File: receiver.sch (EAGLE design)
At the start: 32 parts

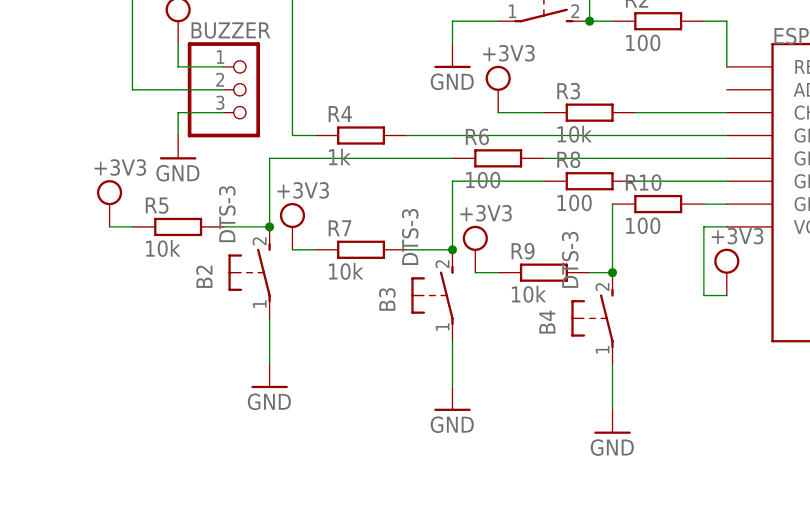
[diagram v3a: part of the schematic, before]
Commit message: Changed 2pins tact switches for 4pins tact switches.
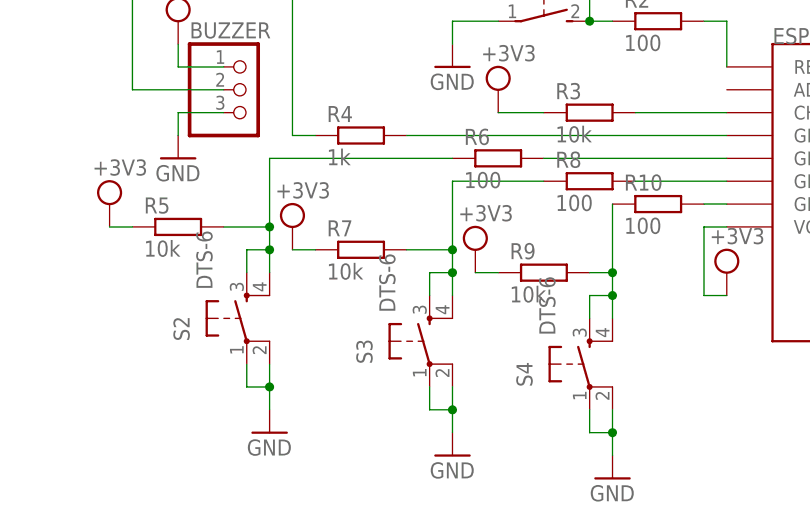
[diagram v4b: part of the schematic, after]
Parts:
- removed B2, B3, B4: DTS-3, switch-tact:DTS-3
- added S2, S3, S4: DTS-6, switch-tact:DTS-6
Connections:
- removed net N$14: B3.2, R7.2, R8.1
- removed net N$8: B4.2, R10.1, R9.2
- new net N$22: R10.1, R9.2, S4.3, S4.4
- new net N$23: R5.2, R6.1, S2.3, S2.4
- net GND: now also S2.1, S2.2, S3.1, S3.2, S4.1, S4.2; no longer B2.1, B3.1, B4.1
- net N$13: now also R7.2, R8.1, S3.3, S3.4; no longer B2.2, R5.2, R6.1
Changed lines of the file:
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@@
 <part name="PROG_USB" library="pinhead" library_urn="urn:adsk.eagle:library:325" deviceset="PINHD-1X4" device="" package3d_urn="urn:adsk.eagle:package:22407/2"/>
 <part name="GND4" library="supply1" library_urn="urn:adsk.eagle:library:371" deviceset="GND" device=""/>
-<part name="B3" library="switch-tact" deviceset="DTS-3" device=""/>
-<part name="B4" library="switch-tact" deviceset="DTS-3" device=""/>
 <part name="R7" library="rcl" library_urn="urn:adsk.eagle:library:334" deviceset="R-EU_" device="0204/5" package3d_urn="urn:adsk.eagle:package:23488/1" value="10k"/>
 <part name="R9" library="rcl" library_urn="urn:adsk.eagle:library:334" deviceset="R-EU_" device="0204/5" package3d_urn="urn:adsk.eagle:package:23488/1" value="10k"/>
@@
 <part name="SUPPLY18" library="supply2" library_urn="urn:adsk.eagle:library:372" deviceset="VCC" device="" value="+3V3"/>
 <part name="SU/SD3V3" library="Pololu Voltage Regulators" deviceset="5V_VOLTAGE_REGULATOR" device=""/>
-<part name="B2" library="switch-tact" deviceset="DTS-3" device=""/>
 <part name="R5" library="rcl" library_urn="urn:adsk.eagle:library:334" deviceset="R-EU_" device="0204/5" package3d_urn="urn:adsk.eagle:package:23488/1" value="10k"/>
 <part name="R6" library="rcl" library_urn="urn:adsk.eagle:library:334" deviceset="R-EU_" device="0204/5" package3d_urn="urn:adsk.eagle:package:23488/1" value="100"/>
@@
 <part name="R14" library="rcl" library_urn="urn:adsk.eagle:library:334" deviceset="R-EU_" device="0204/5" package3d_urn="urn:adsk.eagle:package:23488/1" value="100"/>
 <part name="R2" library="rcl" library_urn="urn:adsk.eagle:library:334" deviceset="R-EU_" device="0204/5" package3d_urn="urn:adsk.eagle:package:23488/1" value="100"/>
+<part name="S2" library="switch-tact" deviceset="DTS-6" device=""/>
+<part name="S3" library="switch-tact" deviceset="DTS-6" device=""/>
+<part name="S4" library="switch-tact" deviceset="DTS-6" device=""/>
 </parts>
 <sheets>
@@
 <instance part="PROG_USB" gate="A" x="86.36" y="96.52"/>
 <instance part="GND4" gate="1" x="78.74" y="86.36"/>
-<instance part="B3" gate="G$1" x="10.16" y="48.26"/>
-<instance part="B4" gate="G$1" x="27.94" y="45.72"/>
 <instance part="R7" gate="G$1" x="0" y="53.34"/>
 <instance part="R9" gate="G$1" x="20.32" y="50.8"/>
@@
 <instance part="S1" gate="G$1" x="109.22" y="50.8" rot="R90"/>
 <instance part="GND2" gate="1" x="119.38" y="45.72"/>
-<instance part="GND10" gate="1" x="27.94" y="33.02"/>
+<instance part="GND10" gate="1" x="27.94" y="27.94"/>
 <instance part="R8" gate="G$1" x="25.4" y="60.96"/>
-<instance part="GND11" gate="1" x="10.16" y="35.56"/>
+<instance part="GND11" gate="1" x="10.16" y="30.48"/>
 <instance part="R11" gate="G$1" x="81.28" y="40.64" rot="R90"/>
 <instance part="GND12" gate="1" x="81.28" y="30.48"/>
@@
 <instance part="SUPPLY18" gate="G$1" x="137.16" y="55.88"/>
 <instance part="SU/SD3V3" gate="J_REG_5V" x="-15.24" y="142.24"/>
-<instance part="B2" gate="G$1" x="-10.16" y="50.8"/>
 <instance part="R5" gate="G$1" x="-20.32" y="55.88"/>
 <instance part="R6" gate="G$1" x="15.24" y="63.5"/>
-<instance part="GND7" gate="1" x="-10.16" y="38.1"/>
+<instance part="GND7" gate="1" x="-10.16" y="33.02"/>
 <instance part="SUPPLY6" gate="G$1" x="-27.94" y="58.42"/>
 <instance part="U$1" gate="G$1" x="-27.94" y="109.22"/>
@@
 <instance part="R14" gate="G$1" x="83.82" y="63.5"/>
 <instance part="R2" gate="G$1" x="33.02" y="78.74"/>
+<instance part="S2" gate="G$1" x="-12.7" y="45.72"/>
+<instance part="S3" gate="G$1" x="7.62" y="43.18"/>
+<instance part="S4" gate="G$1" x="25.4" y="40.64"/>
 </instances>
 <busses>
@@
 </segment>
 <segment>
-<pinref part="B3" gate="G$1" pin="1"/>
 <pinref part="GND11" gate="1" pin="GND"/>
-<wire x1="10.16" y1="43.18" x2="10.16" y2="38.1" width="0.1524" layer="91"/>
+<wire x1="10.16" y1="38.1" x2="10.16" y2="35.56" width="0.1524" layer="91"/>
+<pinref part="S3" gate="G$1" pin="2"/>
+<pinref part="S3" gate="G$1" pin="1"/>
+<wire x1="10.16" y1="35.56" x2="10.16" y2="33.02" width="0.1524" layer="91"/>
+<wire x1="7.62" y1="38.1" x2="7.62" y2="35.56" width="0.1524" layer="91"/>
+<wire x1="7.62" y1="35.56" x2="10.16" y2="35.56" width="0.1524" layer="91"/>
+<junction x="10.16" y="35.56"/>
 </segment>
 <segment>
 <pinref part="GND10" gate="1" pin="GND"/>
-<pinref part="B4" gate="G$1" pin="1"/>
-<wire x1="27.94" y1="35.56" x2="27.94" y2="40.64" width="0.1524" layer="91"/>
+<wire x1="27.94" y1="30.48" x2="27.94" y2="33.02" width="0.1524" layer="91"/>
+<pinref part="S4" gate="G$1" pin="2"/>
+<pinref part="S4" gate="G$1" pin="1"/>
+<wire x1="27.94" y1="33.02" x2="27.94" y2="35.56" width="0.1524" layer="91"/>
+<wire x1="25.4" y1="35.56" x2="25.4" y2="33.02" width="0.1524" layer="91"/>
+<wire x1="25.4" y1="33.02" x2="27.94" y2="33.02" width="0.1524" layer="91"/>
+<junction x="27.94" y="33.02"/>
 </segment>
 <segment>
@@
 </segment>
 <segment>
-<pinref part="B2" gate="G$1" pin="1"/>
 <pinref part="GND7" gate="1" pin="GND"/>
-<wire x1="-10.16" y1="45.72" x2="-10.16" y2="40.64" width="0.1524" layer="91"/>
+<wire x1="-10.16" y1="40.64" x2="-10.16" y2="38.1" width="0.1524" layer="91"/>
+<pinref part="S2" gate="G$1" pin="2"/>
+<pinref part="S2" gate="G$1" pin="1"/>
+<wire x1="-10.16" y1="38.1" x2="-10.16" y2="35.56" width="0.1524" layer="91"/>
+<wire x1="-12.7" y1="40.64" x2="-12.7" y2="38.1" width="0.1524" layer="91"/>
+<wire x1="-12.7" y1="38.1" x2="-10.16" y2="38.1" width="0.1524" layer="91"/>
+<junction x="-10.16" y="38.1"/>
 </segment>
 <segment>
@@
 </segment>
 </net>
-<net name="N$8" class="0">
-<segment>
-<pinref part="B4" gate="G$1" pin="2"/>
-<pinref part="R10" gate="G$1" pin="1"/>
-<wire x1="27.94" y1="50.8" x2="27.94" y2="58.42" width="0.1524" layer="91"/>
-<pinref part="R9" gate="G$1" pin="2"/>
-<wire x1="27.94" y1="50.8" x2="25.4" y2="50.8" width="0.1524" layer="91"/>
-<junction x="27.94" y="50.8"/>
-</segment>
-</net>
 <net name="N$10" class="0">
 <segment>
@@
 </segment>
 </net>
-<net name="N$13" class="0">
-<segment>
-<pinref part="R5" gate="G$1" pin="2"/>
-<wire x1="-15.24" y1="55.88" x2="-10.16" y2="55.88" width="0.1524" layer="91"/>
-<pinref part="B2" gate="G$1" pin="2"/>
-<pinref part="R6" gate="G$1" pin="1"/>
-<wire x1="10.16" y1="63.5" x2="-10.16" y2="63.5" width="0.1524" layer="91"/>
-<wire x1="-10.16" y1="63.5" x2="-10.16" y2="55.88" width="0.1524" layer="91"/>
-<junction x="-10.16" y="55.88"/>
-</segment>
-</net>
 <net name="N$12" class="0">
 <segment>
@@
 <pinref part="ESP-12E" gate="G$1" pin="GPIO14"/>
 <wire x1="20.32" y1="63.5" x2="40.64" y2="63.5" width="0.1524" layer="91"/>
-</segment>
-</net>
-<net name="N$14" class="0">
-<segment>
-<pinref part="B3" gate="G$1" pin="2"/>
-<pinref part="R7" gate="G$1" pin="2"/>
-<wire x1="5.08" y1="53.34" x2="10.16" y2="53.34" width="0.1524" layer="91"/>
-<pinref part="R8" gate="G$1" pin="1"/>
-<wire x1="20.32" y1="60.96" x2="10.16" y2="60.96" width="0.1524" layer="91"/>
-<wire x1="10.16" y1="53.34" x2="10.16" y2="60.96" width="0.1524" layer="91"/>
-<junction x="10.16" y="53.34"/>
 </segment>
 </net>
@@
 </segment>
 </net>
+<net name="N$13" class="0">
+<segment>
+<pinref part="S3" gate="G$1" pin="3"/>
+<wire x1="7.62" y1="48.26" x2="7.62" y2="50.8" width="0.1524" layer="91"/>
+<wire x1="7.62" y1="50.8" x2="10.16" y2="50.8" width="0.1524" layer="91"/>
+<pinref part="S3" gate="G$1" pin="4"/>
+<wire x1="10.16" y1="50.8" x2="10.16" y2="48.26" width="0.1524" layer="91"/>
+<pinref part="R7" gate="G$1" pin="2"/>
+<wire x1="5.08" y1="53.34" x2="10.16" y2="53.34" width="0.1524" layer="91"/>
+<pinref part="R8" gate="G$1" pin="1"/>
+<wire x1="20.32" y1="60.96" x2="10.16" y2="60.96" width="0.1524" layer="91"/>
+<wire x1="10.16" y1="53.34" x2="10.16" y2="60.96" width="0.1524" layer="91"/>
+<wire x1="10.16" y1="50.8" x2="10.16" y2="53.34" width="0.1524" layer="91"/>
+<junction x="10.16" y="50.8"/>
+<junction x="10.16" y="53.34"/>
+</segment>
+</net>
+<net name="N$22" class="0">
+<segment>
+<pinref part="S4" gate="G$1" pin="3"/>
+<wire x1="25.4" y1="45.72" x2="25.4" y2="48.26" width="0.1524" layer="91"/>
+<wire x1="25.4" y1="48.26" x2="27.94" y2="48.26" width="0.1524" layer="91"/>
+<pinref part="S4" gate="G$1" pin="4"/>
+<wire x1="27.94" y1="48.26" x2="27.94" y2="45.72" width="0.1524" layer="91"/>
+<pinref part="R10" gate="G$1" pin="1"/>
+<wire x1="27.94" y1="50.8" x2="27.94" y2="58.42" width="0.1524" layer="91"/>
+<pinref part="R9" gate="G$1" pin="2"/>
+<wire x1="27.94" y1="50.8" x2="25.4" y2="50.8" width="0.1524" layer="91"/>
+<wire x1="27.94" y1="48.26" x2="27.94" y2="50.8" width="0.1524" layer="91"/>
+<junction x="27.94" y="48.26"/>
+<junction x="27.94" y="50.8"/>
+</segment>
+</net>
+<net name="N$23" class="0">
+<segment>
+<pinref part="S2" gate="G$1" pin="4"/>
+<wire x1="-10.16" y1="53.34" x2="-10.16" y2="50.8" width="0.1524" layer="91"/>
+<wire x1="-12.7" y1="53.34" x2="-10.16" y2="53.34" width="0.1524" layer="91"/>
+<pinref part="S2" gate="G$1" pin="3"/>
+<wire x1="-12.7" y1="50.8" x2="-12.7" y2="53.34" width="0.1524" layer="91"/>
+<pinref part="R5" gate="G$1" pin="2"/>
+<pinref part="R6" gate="G$1" pin="1"/>
+<wire x1="-15.24" y1="55.88" x2="-10.16" y2="55.88" width="0.1524" layer="91"/>
+<wire x1="10.16" y1="63.5" x2="-10.16" y2="63.5" width="0.1524" layer="91"/>
+<wire x1="-10.16" y1="63.5" x2="-10.16" y2="55.88" width="0.1524" layer="91"/>
+<wire x1="-10.16" y1="53.34" x2="-10.16" y2="55.88" width="0.1524" layer="91"/>
+<junction x="-10.16" y="53.34"/>
+<junction x="-10.16" y="55.88"/>
+</segment>
+</net>

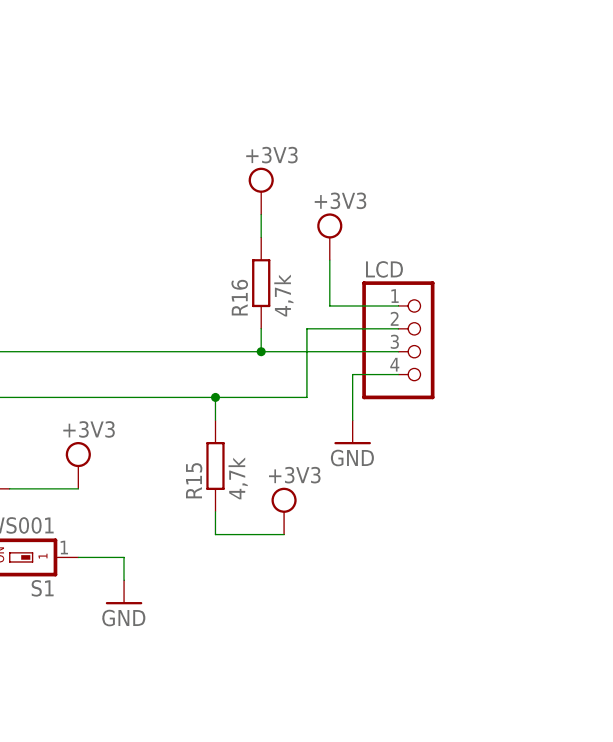
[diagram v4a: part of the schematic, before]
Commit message: Changed OLED socket from 4 pins on 8 pins.
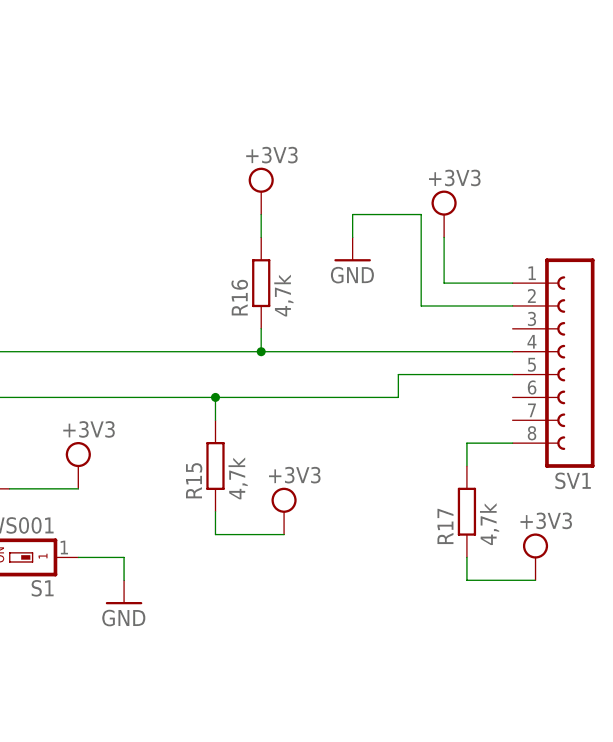
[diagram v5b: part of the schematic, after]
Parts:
- removed LCD: (no value), pinhead:PINHD-1X4
- added R17: 4,7k, rcl:R-EU_0204/5
- added SV1: (no value), con-lsta:FE08-1
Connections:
- new net N$8: SV1.8
- net GND: now also SV1.2; no longer LCD.4
- net SCL: now also SV1.5; no longer LCD.2
- net SDA: now also SV1.4; no longer LCD.3
- net VCC: now also R17.1; no longer LCD.1
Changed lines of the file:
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@@
 <part name="GND1" library="supply1" library_urn="urn:adsk.eagle:library:371" deviceset="GND" device=""/>
 <part name="R3" library="rcl" library_urn="urn:adsk.eagle:library:334" deviceset="R-EU_" device="0204/5" package3d_urn="urn:adsk.eagle:package:23488/1" value="10k"/>
-<part name="LCD" library="pinhead" library_urn="urn:adsk.eagle:library:325" deviceset="PINHD-1X4" device="" package3d_urn="urn:adsk.eagle:package:22407/2"/>
 <part name="GND3" library="supply1" library_urn="urn:adsk.eagle:library:371" deviceset="GND" device=""/>
 <part name="PROG_USB" library="pinhead" library_urn="urn:adsk.eagle:library:325" deviceset="PINHD-1X4" device="" package3d_urn="urn:adsk.eagle:package:22407/2"/>
@@
 <part name="S3" library="switch-tact" deviceset="DTS-6" device=""/>
 <part name="S4" library="switch-tact" deviceset="DTS-6" device=""/>
+<part name="SV1" library="con-lsta" library_urn="urn:adsk.eagle:library:161" deviceset="FE08-1" device="" package3d_urn="urn:adsk.eagle:package:8194/1"/>
+<part name="R17" library="rcl" library_urn="urn:adsk.eagle:library:334" deviceset="R-EU_" device="0204/5" package3d_urn="urn:adsk.eagle:package:23488/1" value="4,7k"/>
+<part name="SUPPLY15" library="supply2" library_urn="urn:adsk.eagle:library:372" deviceset="VCC" device="" value="+3V3"/>
 </parts>
 <sheets>
@@
 <instance part="GND1" gate="1" x="76.2" y="50.8"/>
 <instance part="R3" gate="G$1" x="25.4" y="68.58"/>
-<instance part="LCD" gate="A" x="152.4" y="73.66"/>
-<instance part="GND3" gate="1" x="144.78" y="63.5"/>
+<instance part="GND3" gate="1" x="144.78" y="83.82"/>
 <instance part="PROG_USB" gate="A" x="86.36" y="96.52"/>
 <instance part="GND4" gate="1" x="78.74" y="86.36"/>
@@
 <instance part="SUPPLY11" gate="G$1" x="15.24" y="71.12"/>
 <instance part="SUPPLY12" gate="G$1" x="7.62" y="144.78"/>
-<instance part="SUPPLY7" gate="G$1" x="142.24" y="86.36"/>
+<instance part="SUPPLY7" gate="G$1" x="154.94" y="88.9"/>
 <instance part="SUPPLY4" gate="G$1" x="-7.62" y="55.88"/>
 <instance part="SUPPLY13" gate="G$1" x="12.7" y="53.34"/>
@@
 <instance part="S3" gate="G$1" x="7.62" y="43.18"/>
 <instance part="S4" gate="G$1" x="25.4" y="40.64"/>
+<instance part="SV1" gate="G$1" x="170.18" y="73.66" rot="R180"/>
+<instance part="R17" gate="G$1" x="157.48" y="55.88" rot="R90"/>
+<instance part="SUPPLY15" gate="G$1" x="165.1" y="50.8"/>
 </instances>
 <busses>
@@
 </segment>
 <segment>
-<pinref part="LCD" gate="A" pin="1"/>
-<wire x1="149.86" y1="78.74" x2="142.24" y2="78.74" width="0.1524" layer="91"/>
-<wire x1="142.24" y1="78.74" x2="142.24" y2="83.82" width="0.1524" layer="91"/>
+<wire x1="162.56" y1="81.28" x2="154.94" y2="81.28" width="0.1524" layer="91"/>
+<wire x1="154.94" y1="81.28" x2="154.94" y2="86.36" width="0.1524" layer="91"/>
 <pinref part="SUPPLY7" gate="G$1" pin="VCC"/>
 </segment>
@@
 <pinref part="SUPPLY10" gate="G$1" pin="VCC"/>
 </segment>
+<segment>
+<pinref part="R17" gate="G$1" pin="1"/>
+<wire x1="157.48" y1="50.8" x2="157.48" y2="48.26" width="0.1524" layer="91"/>
+<wire x1="157.48" y1="48.26" x2="165.1" y2="48.26" width="0.1524" layer="91"/>
+<pinref part="SUPPLY15" gate="G$1" pin="VCC"/>
+</segment>
 </net>
 <net name="GND" class="0">
@@
 <wire x1="73.66" y1="55.88" x2="76.2" y2="55.88" width="0.1524" layer="91"/>
 <wire x1="76.2" y1="55.88" x2="76.2" y2="53.34" width="0.1524" layer="91"/>
-</segment>
-<segment>
-<pinref part="LCD" gate="A" pin="4"/>
-<wire x1="149.86" y1="71.12" x2="144.78" y2="71.12" width="0.1524" layer="91"/>
-<wire x1="144.78" y1="71.12" x2="144.78" y2="66.04" width="0.1524" layer="91"/>
-<pinref part="GND3" gate="1" pin="GND"/>
 </segment>
 <segment>
@@
 <wire x1="-20.32" y1="68.58" x2="-20.32" y2="66.04" width="0.1524" layer="91"/>
 </segment>
+<segment>
+<pinref part="SV1" gate="G$1" pin="2"/>
+<wire x1="162.56" y1="78.74" x2="152.4" y2="78.74" width="0.1524" layer="91"/>
+<wire x1="152.4" y1="78.74" x2="152.4" y2="88.9" width="0.1524" layer="91"/>
+<wire x1="152.4" y1="88.9" x2="144.78" y2="88.9" width="0.1524" layer="91"/>
+<pinref part="GND3" gate="1" pin="GND"/>
+<wire x1="144.78" y1="88.9" x2="144.78" y2="86.36" width="0.1524" layer="91"/>
+</segment>
 </net>
 <net name="N$1" class="0">
@@
 <net name="SCL" class="0">
 <segment>
-<pinref part="LCD" gate="A" pin="2"/>
-<wire x1="149.86" y1="76.2" x2="139.7" y2="76.2" width="0.1524" layer="91"/>
-<wire x1="129.54" y1="68.58" x2="139.7" y2="68.58" width="0.1524" layer="91"/>
-<wire x1="139.7" y1="68.58" x2="139.7" y2="76.2" width="0.1524" layer="91"/>
 <label x="93.98" y="68.58" size="1.778" layer="95"/>
 <pinref part="R15" gate="G$1" pin="2"/>
@@
 <pinref part="ESP-12E" gate="G$1" pin="GPIO5"/>
 <wire x1="129.54" y1="68.58" x2="73.66" y2="68.58" width="0.1524" layer="91"/>
+<wire x1="129.54" y1="68.58" x2="149.86" y2="68.58" width="0.1524" layer="91"/>
+<wire x1="149.86" y1="68.58" x2="149.86" y2="71.12" width="0.1524" layer="91"/>
+<pinref part="SV1" gate="G$1" pin="5"/>
+<wire x1="149.86" y1="71.12" x2="162.56" y2="71.12" width="0.1524" layer="91"/>
 </segment>
 </net>
@@
 <wire x1="134.62" y1="76.2" x2="134.62" y2="73.66" width="0.1524" layer="91"/>
 <wire x1="78.74" y1="73.66" x2="134.62" y2="73.66" width="0.1524" layer="91"/>
-<pinref part="LCD" gate="A" pin="3"/>
-<wire x1="149.86" y1="73.66" x2="134.62" y2="73.66" width="0.1524" layer="91"/>
+<wire x1="162.56" y1="73.66" x2="134.62" y2="73.66" width="0.1524" layer="91"/>
 <junction x="134.62" y="73.66"/>
+<pinref part="SV1" gate="G$1" pin="4"/>
 </segment>
 </net>
@@
 </segment>
 </net>
+<net name="N$8" class="0">
+<segment>
+<pinref part="SV1" gate="G$1" pin="8"/>
+<wire x1="162.56" y1="63.5" x2="157.48" y2="63.5" width="0.1524" layer="91"/>
+<wire x1="157.48" y1="63.5" x2="157.48" y2="60.96" width="0.1524" layer="91"/>
+</segment>
+</net>
